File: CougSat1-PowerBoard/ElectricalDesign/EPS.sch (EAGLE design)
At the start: 251 parts, among them J1 PV0, J2 PV1, J3 PV2, J4 PV3, J5 Umbilical, J6 SWD, J7 CougSat Card, J8 Deployables, Q1 NTLUD3A50PZ, Q10 DMN2008LFU, Q11 DMN2008LFU, Q12 CSD25402Q3A, Q13 CSD25402Q3A, Q14 NTLUD3A50PZ, Q15 NTLUD3A50PZ, Q16 NTLUD3A50PZ, Q17 NTLUD3A50PZ, Q18 NTLUD3A50PZ, Q19 NTLUD3A50PZ, Q2 NTLUD3A50PZ, Q20 NTLUD3A50PZ, Q21 NTLUD3A50PZ, Q22 NTLUD3A50PZ, Q23 CSD25402Q3A, Q24 CSD25402Q3A, Q25 DMN53D0L, Q26 NTLUD3A50PZ, Q27 NTLUD3A50PZ, Q28 NTLUD3A50PZ, Q29 NTLUD3A50PZ, Q3 NTLUD3A50PZ, Q30 NTLUD3A50PZ, Q31 NTLUD3A50PZ, Q32 NTLUD3A50PZ, Q33 NTLUD3A50PZ, Q34 NTLUD3A50PZ, Q35 NTLUD3A50PZ, Q36 NTLUD3A50PZ, Q37 NTLUD3A50PZ, Q38 NTLUD3A50PZ, Q39 NTLUD3A50PZ, Q4 NTLUD3A50PZ, Q40 NTLUD3A50PZ, Q41 NTLUD3A50PZ, Q42 NTLUD3A50PZ, Q43 NTLUD3A50PZ, Q5 NTLUD3A50PZ, Q6 NTLUD3A50PZ, Q7 NTLUD3A50PZ, Q8 NTLUD3A50PZ, Q9 NTLUD3A50PZ, SW1 D2MQ-1-TL, U1 BQ29700, U10 LTC2499, U11 LTC2499, U12 LTC2499, U13 LTC2499, U14 MCP1501-18, U15 LTC2499, U2 BQ29700, U3 TPS64200, U4 TPS64200, U5 STM32L476RGT, U6 TCA9535R, U7 SN74LVC244AR, U8 TCA9535R, U9 LTC2499

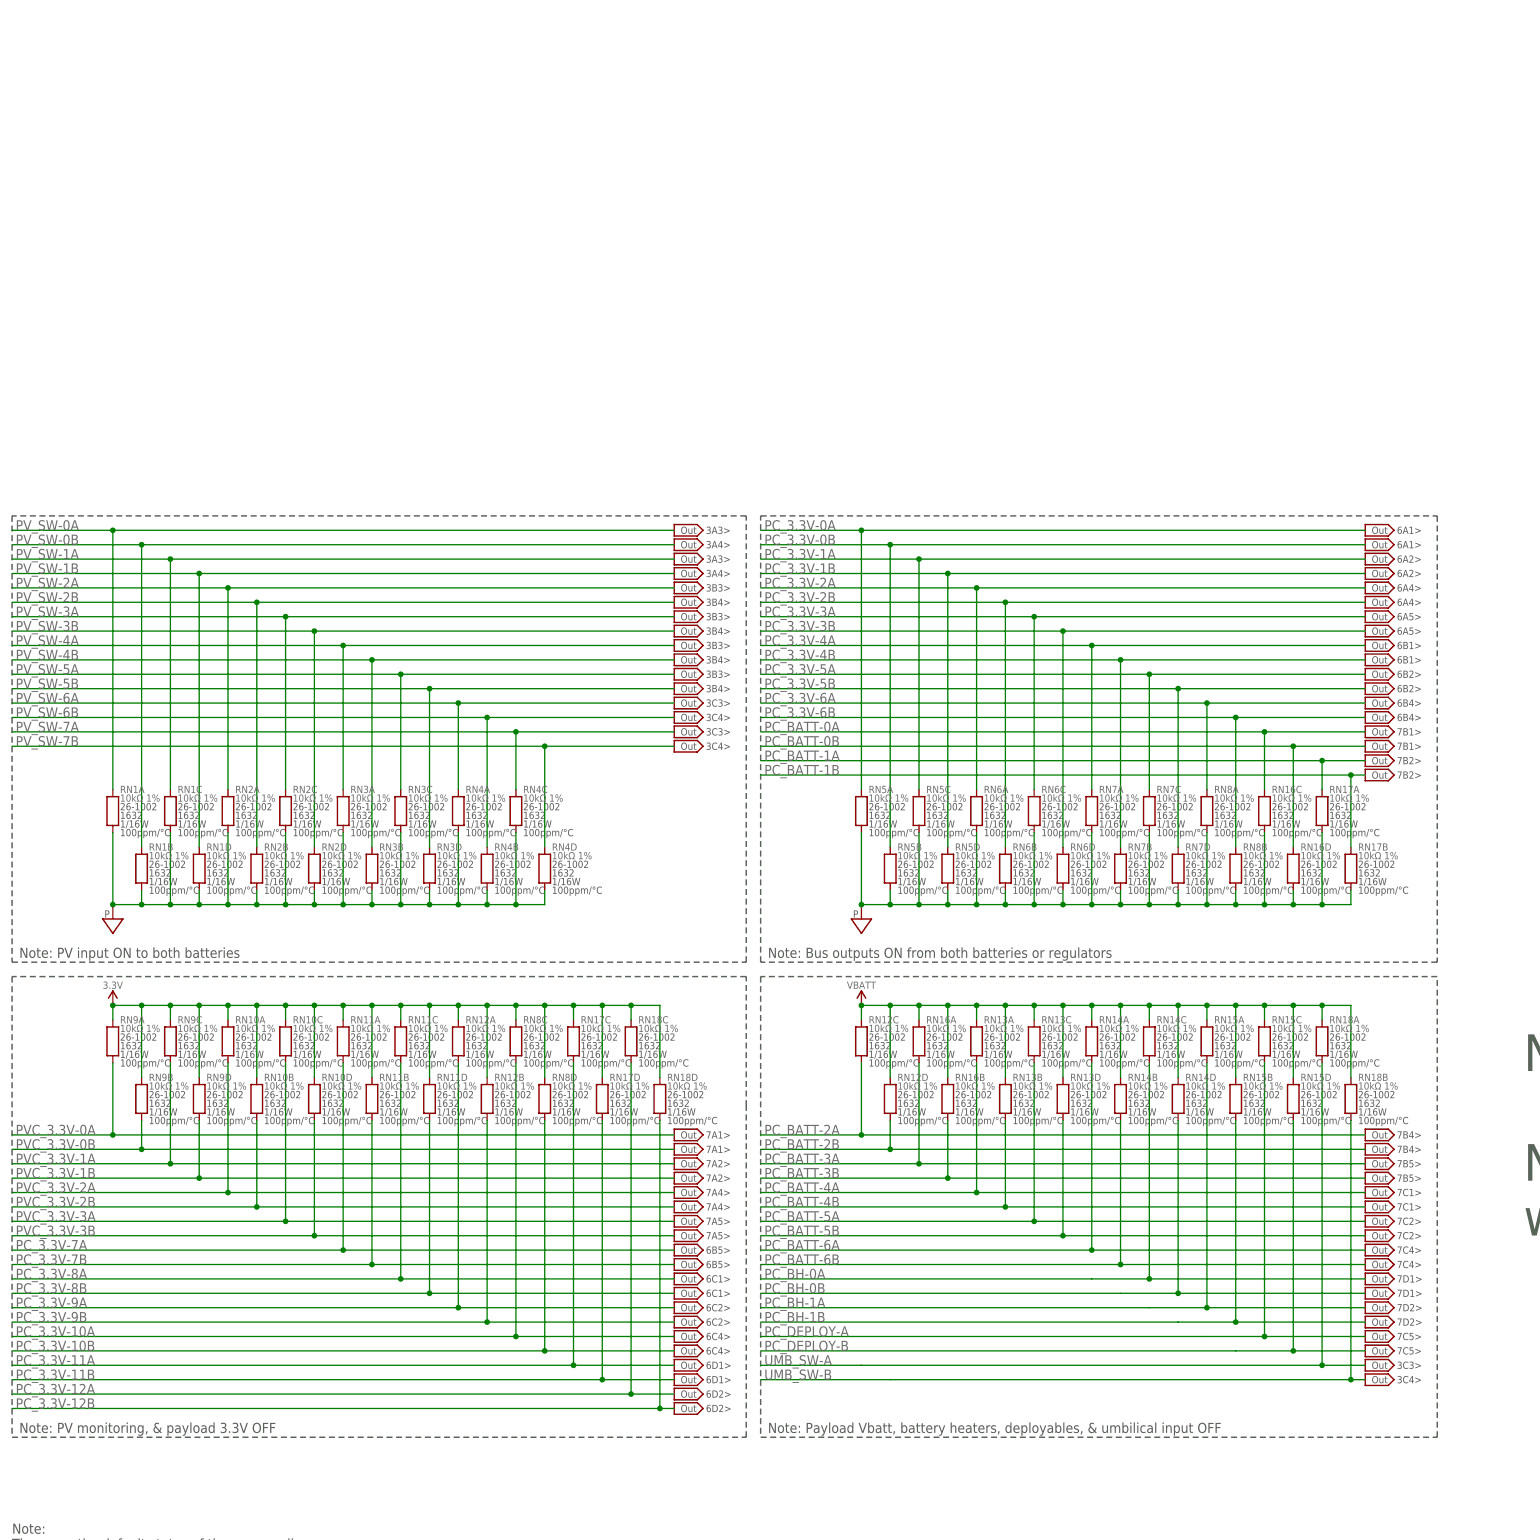
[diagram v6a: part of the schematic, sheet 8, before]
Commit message: Laid Out All Distribution and Output Current Sensing
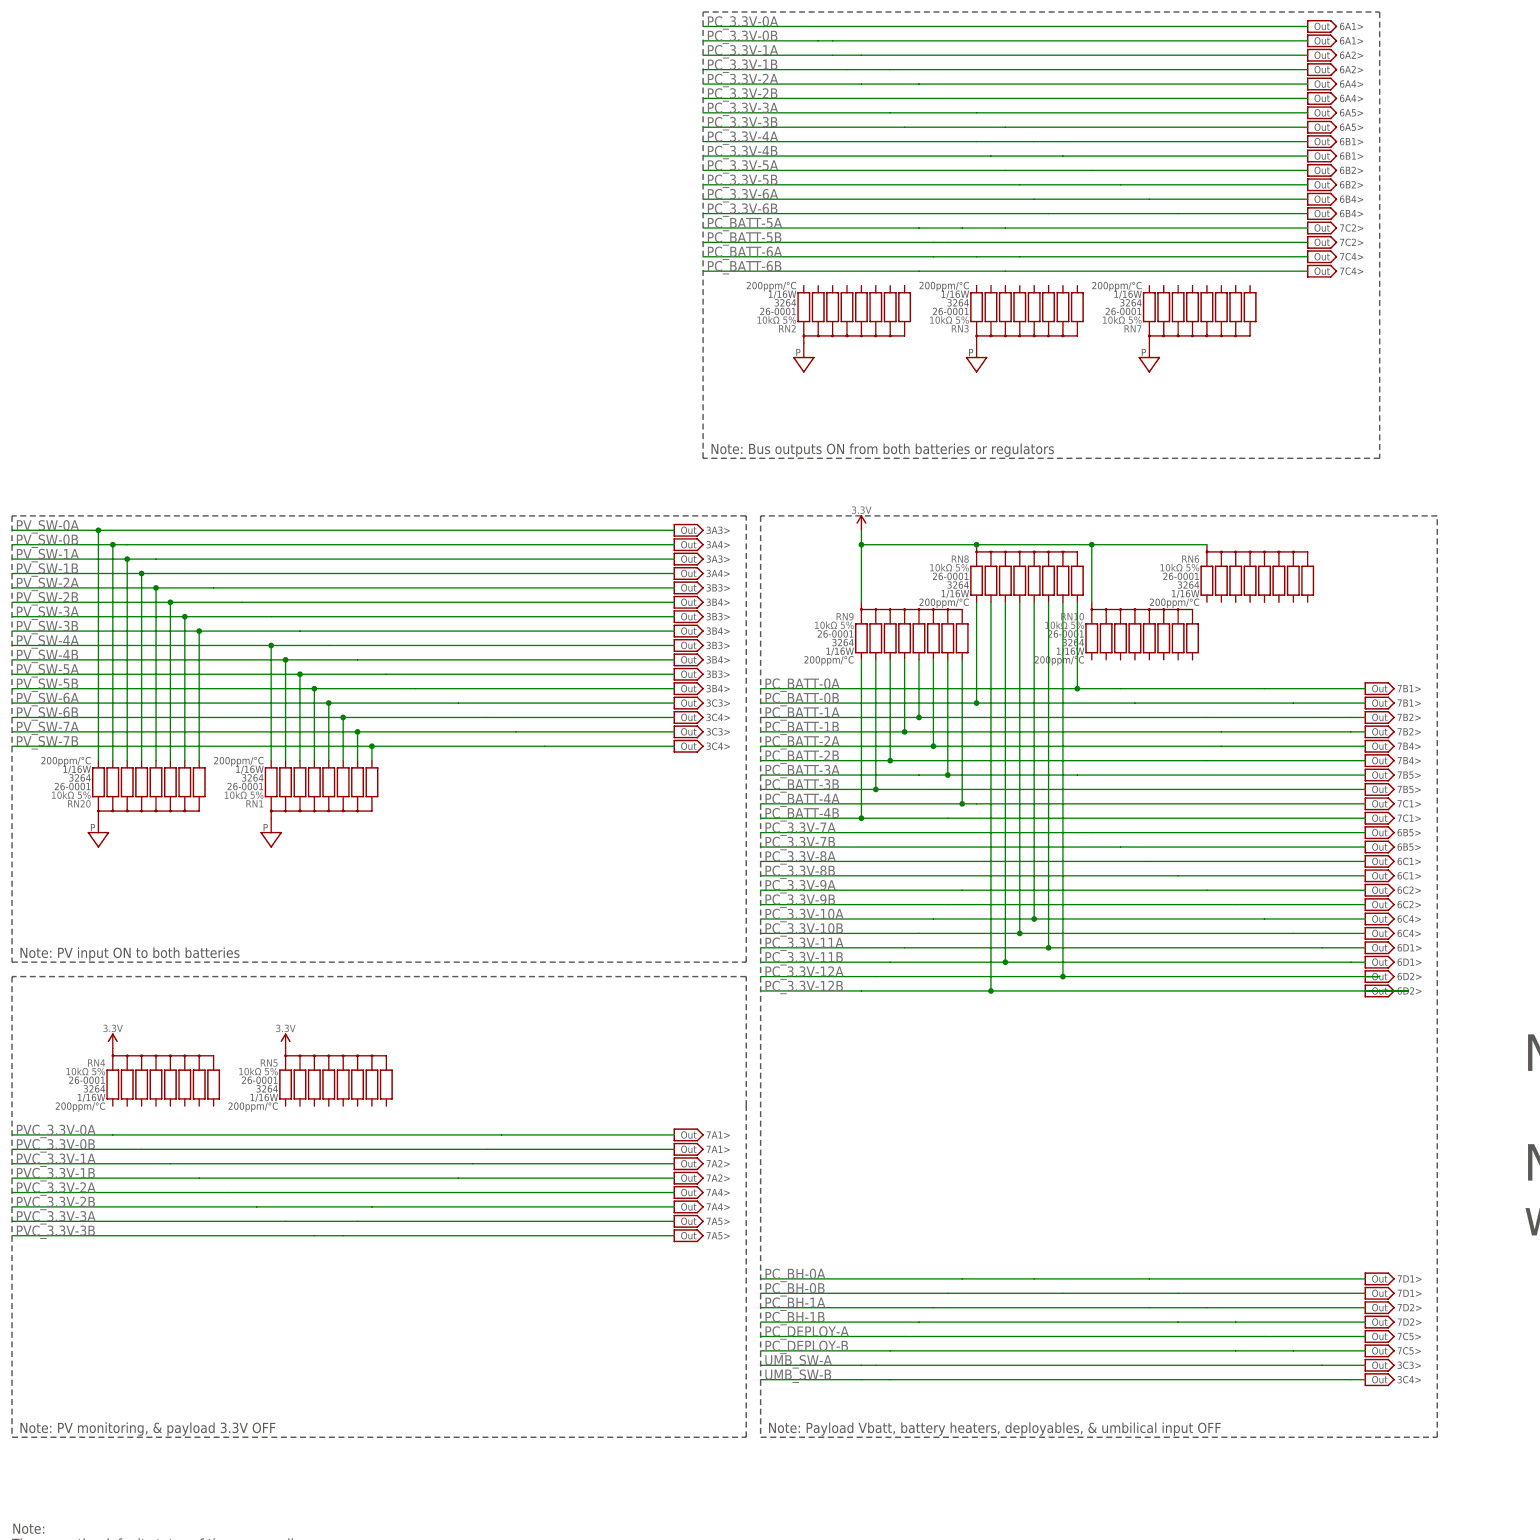
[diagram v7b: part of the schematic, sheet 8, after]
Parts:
- removed RN11, RN12, RN13, RN14, RN15, RN16, RN17, RN18: 10kΩ 1%, CougsInSpace-Resistors:RES-4-V-10K-1632
- added RN20: 10kΩ 5%, CougsInSpace-Resistors:RES_BUS-10-10K-3264
- RN1, RN10, RN2, RN3, RN4, RN5, RN6, RN7, RN8, RN9: value 10kΩ 1% -> 10kΩ 5%; device CougsInSpace-Resistors:RES-4-V-10K-1632 -> CougsInSpace-Resistors:RES_BUS-10-10K-3264
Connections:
- net 3.3V: now also RN10.C, RN4.C, RN5.C, RN6.C, RN8.C, RN9.C, U15.CA0; no longer RN10A.2, RN10B.2, RN10C.2, RN10D.2, RN11A.2, RN11B.2, RN11C.2, RN11D.2, RN12A.2, RN12B.2, RN17C.2, RN17D.2, RN18C.2, RN18D.2, RN8C.2, RN8D.2, RN9A.2, RN9B.2, RN9C.2, RN9D.2, U11.CA0
- net BUS_JTAG_TCK: now also U7E1.A4; no longer U7E1.A1
- net BUS_JTAG_TDI: now also U7E1.A3; no longer U7E1.A2
- net BUS_JTAG_TMS: now also U7E1.A2; no longer U7E1.A3
- net DGND: now also U11.CA0, U15.CA1, U7E1.A1, U7E1.Y1; no longer U11.CA1, U15.CA0, U7E1.A4, U7E1.Y4
- net I_3.3V-10: now also U11.CH14
- net I_3.3V-11: now also U11.CH12
- net I_3.3V-12: now also U10.CH10
- net I_3.3V-8: now also U11.CH9
- net I_3.3V-9: now also U11.CH10
- net I_BATT-0: now also U10.CH14
- net I_BATT-1: now also U10.CH4
- net I_BATT-2: now also U10.CH0
- net I_BATT-3: now also U10.CH9
- net I_BATT-4: now also U10.CH2
- net I_BATT-5: now also U10.CH7
- net I_BATT-6: now also U10.CH13
- net JTAG_TCK: now also U7E1.Y4; no longer U7E1.Y1
- net JTAG_TDI: now also U7E1.Y3; no longer U7E1.Y2
- net JTAG_TMS: now also U7E1.Y2; no longer U7E1.Y3
- net PC_3.3V-0A: no longer RN5A.2
- net PC_3.3V-0B: no longer RN5B.2
- net PC_3.3V-10A: now also RN8.5; no longer RN8C.1
- net PC_3.3V-10B: now also RN8.4; no longer RN8D.1
- net PC_3.3V-11A: now also RN8.6; no longer RN17C.1
- net PC_3.3V-11B: now also RN8.3; no longer RN17D.1
- net PC_3.3V-12A: now also RN8.7; no longer RN18C.1
- net PC_3.3V-12B: now also RN8.2; no longer RN18D.1
- net PC_3.3V-1A: no longer RN5C.2
- net PC_3.3V-1B: no longer RN5D.2
- net PC_3.3V-2A: no longer RN6A.2
- net PC_3.3V-2B: no longer RN6B.2
- net PC_3.3V-3A: no longer RN6C.2
- net PC_3.3V-3B: no longer RN6D.2
- net PC_3.3V-4A: no longer RN7A.2
- net PC_3.3V-4B: no longer RN7B.2
- net PC_3.3V-5A: no longer RN7C.2
- net PC_3.3V-5B: no longer RN7D.2
- net PC_3.3V-6A: no longer RN8A.2
- net PC_3.3V-6B: no longer RN8B.2
- net PC_3.3V-7A: no longer RN11A.1
- net PC_3.3V-7B: no longer RN11B.1
- net PC_3.3V-8A: no longer RN11C.1
- net PC_3.3V-8B: no longer RN11D.1
- net PC_3.3V-9A: no longer RN12A.1
- net PC_3.3V-9B: no longer RN12B.1
- net PC_BATT-0A: now also RN8.8; no longer RN16C.2
- net PC_BATT-0B: now also RN8.1; no longer RN16D.2
- net PC_BATT-1A: now also RN9.5; no longer RN17A.2
- net PC_BATT-1B: now also RN9.4; no longer RN17B.2
- net PC_BATT-2A: now also RN9.6; no longer RN12C.1
- net PC_BATT-2B: now also RN9.3; no longer RN12D.1
- net PC_BATT-3A: now also RN9.7; no longer RN16A.1
- net PC_BATT-3B: now also RN9.2; no longer RN16B.1
- net PC_BATT-4A: now also RN9.8; no longer RN13A.1
- net PC_BATT-4B: now also RN9.1; no longer RN13B.1
- net PC_BATT-5A: no longer RN13C.1
- net PC_BATT-5B: no longer RN13D.1
- net PC_BATT-6A: no longer RN14A.1
- net PC_BATT-6B: no longer RN14B.1
- net PC_BH-0A: no longer RN14C.1
- net PC_BH-0B: no longer RN14D.1
- net PC_BH-1A: no longer RN15A.1
- net PC_BH-1B: no longer RN15B.1
- net PC_DEPLOY-A: no longer RN15C.1
- net PC_DEPLOY-B: no longer RN15D.1
- net PGND: now also RN1.C, RN2.C, RN20.C, RN3.C, RN7.C; no longer RN16C.1, RN16D.1, RN17A.1, RN17B.1, RN1A.1, RN1B.1, RN1C.1, RN1D.1, RN2A.1, RN2B.1, RN2C.1, RN2D.1, RN3A.1, RN3B.1, RN3C.1, RN3D.1, RN4A.1, RN4B.1, RN4C.1, RN4D.1, RN5A.1, RN5B.1, RN5C.1, RN5D.1, RN6A.1, RN6B.1, RN6C.1, RN6D.1, RN7A.1, RN7B.1, RN7C.1, RN7D.1, RN8A.1, RN8B.1
- net PR_3.3V-10: now also U11.CH15
- net PR_3.3V-11: now also U11.CH13
- net PR_3.3V-12: now also U10.CH11
- net PR_3.3V-8: now also U11.CH8
- net PR_3.3V-9: now also U11.CH11
- net PR_BATT-0: now also U10.CH15
- net PR_BATT-1: now also U10.CH5
- net PR_BATT-2: now also U10.CH1
- net PR_BATT-3: now also U10.CH8
- net PR_BATT-4: now also U10.CH3
- net PR_BATT-5: now also U10.CH6
- net PR_BATT-6: now also U10.CH12
- net PVC_3.3V-0A: no longer RN9A.1
- net PVC_3.3V-0B: no longer RN9B.1
- net PVC_3.3V-1A: no longer RN9C.1
- net PVC_3.3V-1B: no longer RN9D.1
- net PVC_3.3V-2A: no longer RN10A.1
- net PVC_3.3V-2B: no longer RN10B.1
- net PVC_3.3V-3A: no longer RN10C.1
- net PVC_3.3V-3B: no longer RN10D.1
- net PVI_3.3V-2: now also U11.CH3
- net PVI_3.3V-3: now also U11.CH1
- net PV_3.3V-2: now also U11.CH2
- net PV_3.3V-3: now also U11.CH0
- net PV_SW-0A: now also RN20.1; no longer RN1A.2
- net PV_SW-0B: now also RN20.2; no longer RN1B.2
- net PV_SW-1A: now also RN20.3; no longer RN1C.2
- net PV_SW-1B: now also RN20.4; no longer RN1D.2
- net PV_SW-2A: now also RN20.5; no longer RN2A.2
- net PV_SW-2B: now also RN20.6; no longer RN2B.2
- net PV_SW-3A: now also RN20.7; no longer RN2C.2
- net PV_SW-3B: now also RN20.8; no longer RN2D.2
- net PV_SW-4A: now also RN1.1; no longer RN3A.2
- net PV_SW-4B: now also RN1.2; no longer RN3B.2
- net PV_SW-5A: now also RN1.3; no longer RN3C.2
- net PV_SW-5B: now also RN1.4; no longer RN3D.2
- net PV_SW-6A: now also RN1.5; no longer RN4A.2
- net PV_SW-6B: now also RN1.6; no longer RN4B.2
- net PV_SW-7A: now also RN1.7; no longer RN4C.2
- net PV_SW-7B: now also RN1.8; no longer RN4D.2
- net UMB_SW-A: no longer RN18A.1
- net UMB_SW-B: no longer RN18B.1
- net VBATT: no longer RN12C.2, RN12D.2, RN13A.2, RN13B.2, RN13C.2, RN13D.2, RN14A.2, RN14B.2, RN14C.2, RN14D.2, RN15A.2, RN15B.2, RN15C.2, RN15D.2, RN16A.2, RN16B.2, RN18A.2, RN18B.2
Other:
- note added: "<10A5"
- note added: "<6C5 <10A5"
- note added: "<6D5 <10A3"
- note added: "<6D5 <10A5"
- note added: "Note: Fix all off sheet designators linked to this sheet (JTAG too) Note: All signals above are GPIO, connect to any GPIO bank, whichever is best for routing"
- note added: "PR_BATT-0: 250mA"
- note added: "PR_BATT-1: 0mA"
- note added: "PR_BATT-2: 0mA"
- note added: "PR_BATT-5: 300mA"
- note added: "PR_BATT-6: 400mA"
- note added: "todo"
- note removed: "<6D5 <9xx"
- note removed: "<7B2"
- note removed: "<7B4"
- note removed: "<7C1"
- note removed: "<7C2"
- note removed: "Note: Fix all off sheet designators linked to this sheet Note: All signals above are GPIO, connect to any GPIO bank, whichever is best for routing"
- note removed: "PR_BATT-0: 300mA"
- note removed: "PR_BATT-1: 400mA"
- note removed: "PR_BATT-2: 250mA"
- note removed: "PR_BATT-5: 0mA"
- note removed: "PR_BATT-6: 0mA"

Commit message: Laid Out Distribution Control Signals
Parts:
- added R69, R81, R82, R83, R84, R85: 10kΩ 0.1%, CougsInSpace-Resistors:RES-V-10K-1608
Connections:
- net BUS_I2C0_IRQ: now also U5B.PB8
- net CTRL_SYNC: now also U5B.PB9
- net PC_3.3V-0A: now also R69.2, U6.P12
- net PC_3.3V-0B: now also R81.2, U6.P11
- net PC_3.3V-10A: now also U5B.PB2
- net PC_3.3V-10B: now also U5B.PB1
- net PC_3.3V-11A: now also U5B.PB0
- net PC_3.3V-11B: now also U5C.PC5
- net PC_3.3V-12A: now also U5C.PC4
- net PC_3.3V-12B: now also U5A.PA7
- net PC_3.3V-1A: now also R82.2, U6.P10
- net PC_3.3V-1B: now also R83.2, U6.P07
- net PC_3.3V-2A: now also RN2.1, U5C.PC12
- net PC_3.3V-2B: now also RN2.8, U5C.PC11
- net PC_3.3V-3A: now also RN2.2, U5C.PC10
- net PC_3.3V-3B: now also RN2.7, U5A.PA12
- net PC_3.3V-4A: now also RN2.3, U5A.PA11
- net PC_3.3V-4B: now also RN2.6, U5A.PA10
- net PC_3.3V-5A: now also RN2.4, U5A.PA9
- net PC_3.3V-5B: now also RN2.5, U5A.PA8
- net PC_3.3V-6A: now also R84.2, U5C.PC9
- net PC_3.3V-6B: now also R85.2, U5C.PC8
- net PC_3.3V-7A: now also RN10.2, U5C.PC7
- net PC_3.3V-7B: now also RN10.8, U5C.PC6
- net PC_3.3V-8A: now also RN10.3, U5B.PB15
- net PC_3.3V-8B: now also RN10.7, U5B.PB14
- net PC_3.3V-9A: now also RN10.4, U5B.PB13
- net PC_3.3V-9B: now also RN10.6, U5B.PB12
- net PC_BATT-0A: now also U5A.PA6
- net PC_BATT-0B: now also U5A.PA5
- net PC_BATT-1A: now also U5A.PA4
- net PC_BATT-1B: now also U5A.PA3
- net PC_BATT-2A: now also U5C.PC2
- net PC_BATT-2B: now also U5C.PC3
- net PC_BATT-3A: now also U5A.PA0
- net PC_BATT-3B: now also U5A.PA1
- net PC_BATT-4A: now also U5A.PA2
- net PC_BATT-4B: now also U5BASE.PH1-OSC_OUT
- net PC_BATT-5A: now also U5BASE.PH0-OSC_IN
- net PC_BATT-5B: now also U5C.PC15
- net PC_BATT-6A: now also U5C.PC14
- net PC_BATT-6B: now also U5C.PC13
- net PGND: now also R69.1, R81.1, R82.1, R83.1, R84.1, R85.1
- net PVC_3.3V-2A: now also U6.P02
- net PVC_3.3V-2B: now also U6.P01
- net PV_SW-4A: now also U6.P13, U6.P14
- net PV_SW-4B: now also U6.P00
- net PV_SW-5A: now also U6.P15
- net PV_SW-5B: now also U6.P17
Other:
- note added: "<7C1"
- note added: "<7C2"
